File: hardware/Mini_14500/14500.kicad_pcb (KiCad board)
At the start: 2 copper layers, 92.8 x 16 mm, 49 parts, among them J2 Battery, J3 GPIO, J4 USB_B_Micro, J5 Power, J6 LEDs, J7 GPIO, Q1 BSS806N, Q2 BSS806N, Q3 BSS806N, Q4 BSS806N, SW1 Mode, SW2 Power, U1 STM32L072KZUx, U2 AP2210N-3.3TRG1, U3 MCP73831T-2ACI_OT, U4 ESD7002WTT1G

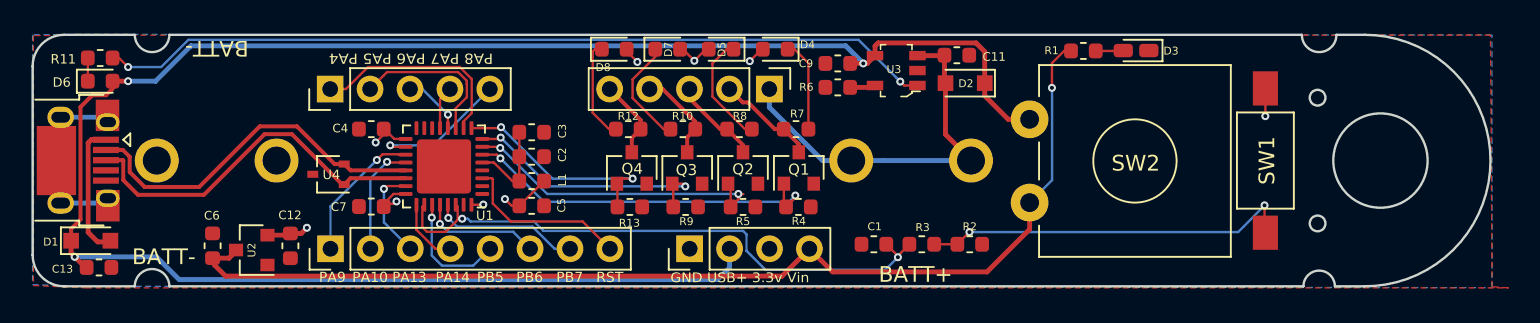
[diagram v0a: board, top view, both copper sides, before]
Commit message: Adjust space around battery terminals.
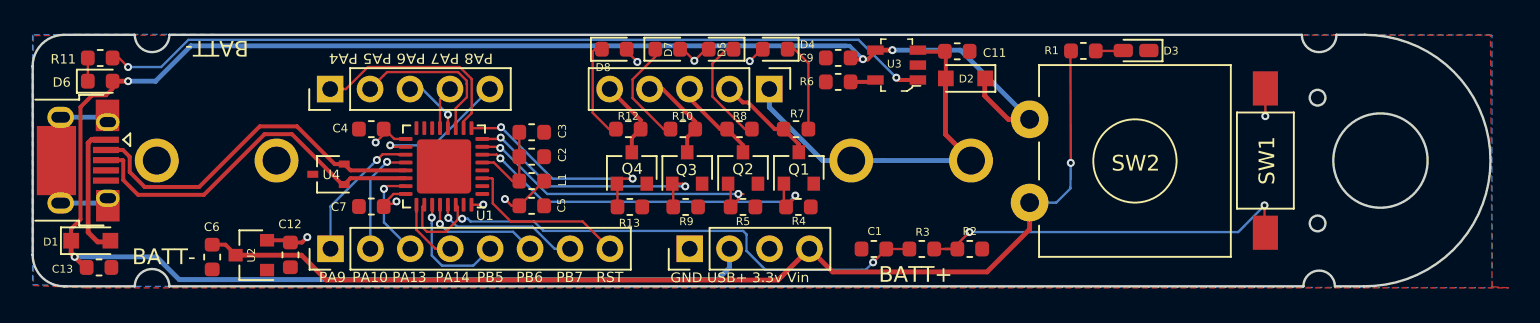
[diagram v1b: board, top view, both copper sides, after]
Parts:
- added REF**: OSHW-Symbol_6.7x6mm_SilkScreen, Symbol:OSHW-Symbol_6.7x6mm_SilkScreen, B.Cu at (127.8, 99.7)
- R11: value 430 -> 330
- moved C6 0.72 mm to (69.5, 106.1), turned to 270 degrees
- moved C12 0.58 mm to (74.5, 106.0)
- moved U3 0.35 mm to (113.1, 93.9)
- moved C9 0.35 mm to (109.3, 93.5)
- moved R6 0.35 mm to (109.3, 95.0)
- moved U2 0.33 mm to (72.0, 106.0)
- moved D2 0.30 mm to (117.5, 94.8)
- moved C1 0.30 mm to (111.6, 105.6)
- moved R2 0.30 mm to (117.7, 105.6)
- moved R3 0.30 mm to (114.7, 105.6)
- moved C11 0.25 mm to (116.9, 93.0)
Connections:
- J4 pad 4: (no net) -> Net-(J4-Pad4)
- U1 pad 1: (no net) -> Net-(U1-Pad1)
- U1 pad 14: (no net) -> Net-(U1-Pad14)
- U1 pad 15: (no net) -> Net-(U1-Pad15)
- U1 pad 2: (no net) -> Net-(U1-Pad2)
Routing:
- net /VUSB: track 122.8 -> 124.4 mm, vias 3 -> 4
- net /BUTTON: track 38.0 -> 37.2 mm
- net Net-(R2-Pad1): track 24.1 -> 24.7 mm
- net /VIN: track 69.4 -> 68.9 mm
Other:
- board text added: "rev 1"
- board text removed: "rev 1a"
